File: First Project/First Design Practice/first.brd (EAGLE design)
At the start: 118.1 x 55.5 mm, 6 parts, among them U1 ARDUINOR3-BPLACE

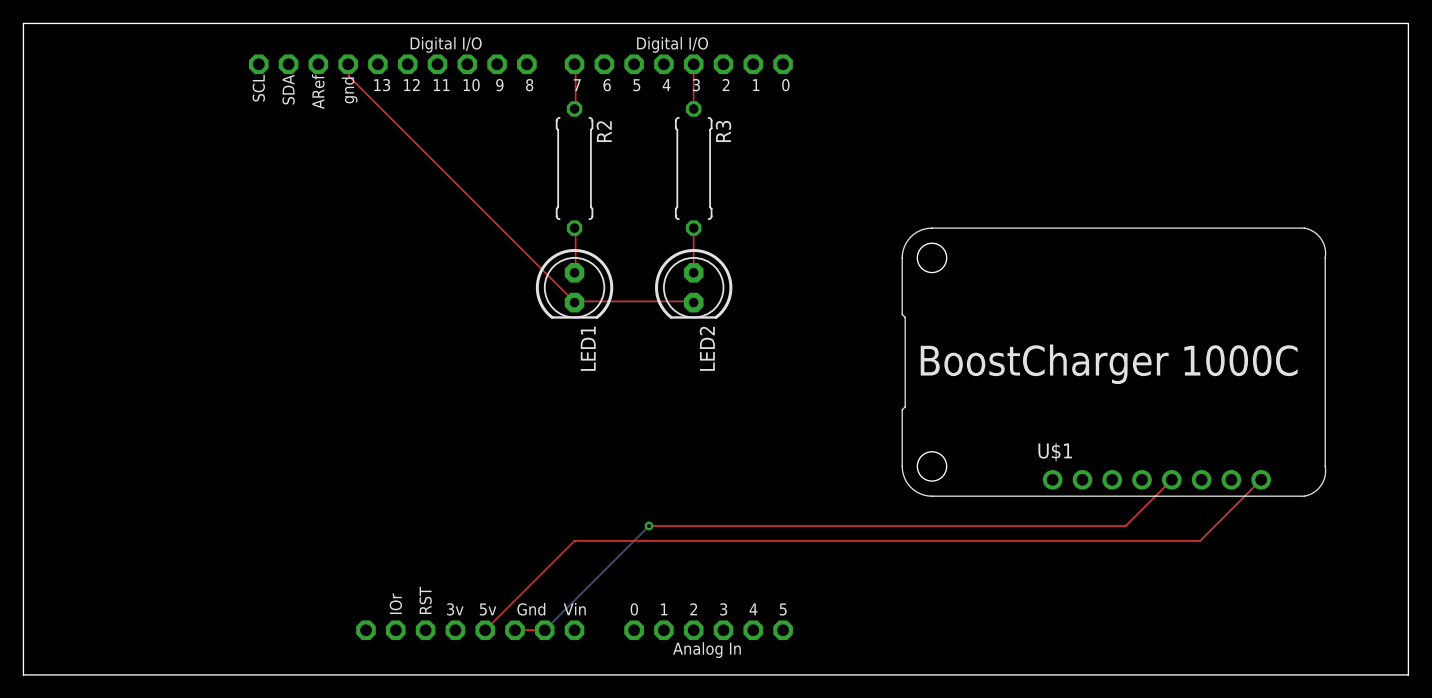
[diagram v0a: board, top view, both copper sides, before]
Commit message: Added Experimental Boards/ Gravity Board/ Home Automation Boards
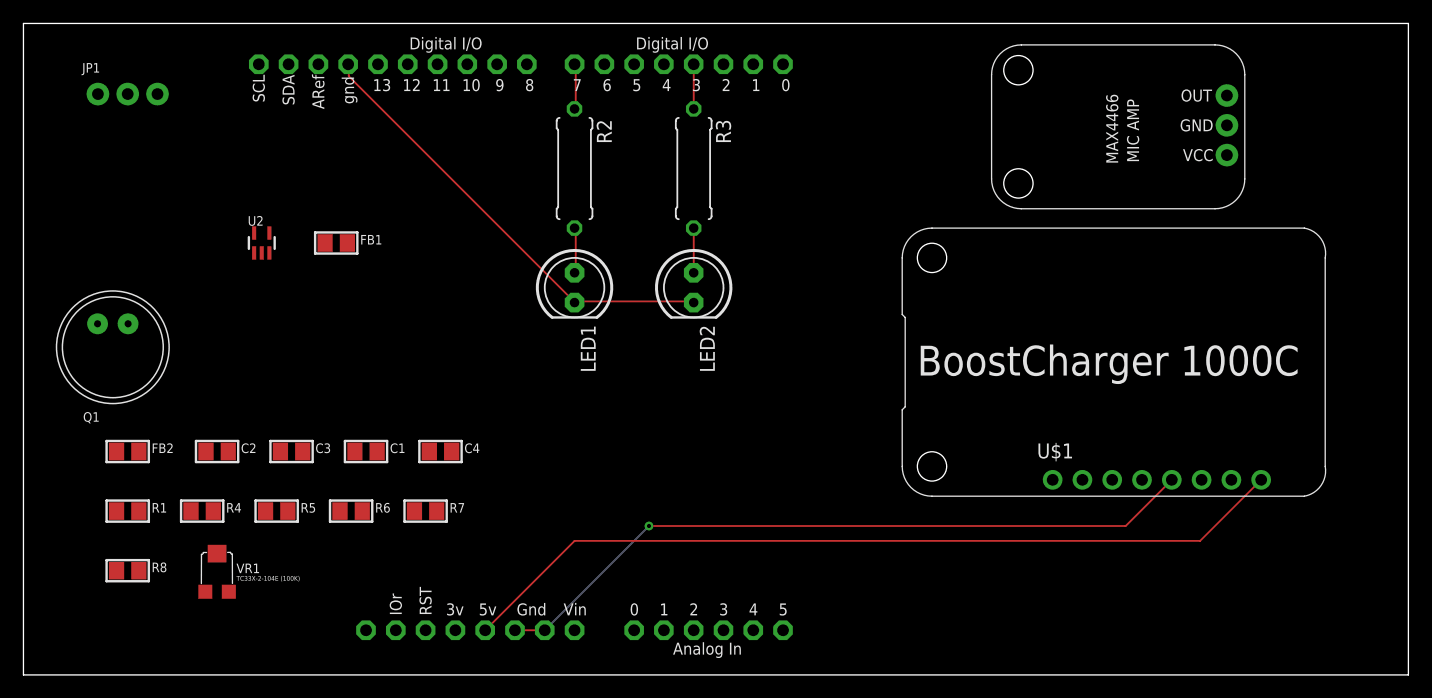
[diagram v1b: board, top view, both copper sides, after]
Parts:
- added C1: 0.1µF, microbuilder:0805
- added C2: 0.01uF, microbuilder:0805
- added C3: 100pF, microbuilder:0805
- added C4: 10uF, microbuilder:0805
- added FB1, FB2: FERRITE, microbuilder:0805
- added JP1: (no value), microbuilder:1X03_ROUND_76
- added Q1: CMA-4544PF-W, microbuilder:ELECTRET_9.7
- added R1, R4, R5: 1K, microbuilder:0805
- added R6, R7: 1M, microbuilder:0805
- added R8: 22K, microbuilder:0805
- added U$11: MAX4466-MIC-AMP, untitled:MAX4466
- added U2: MAX4466EXK+T, microbuilder:SC70-5
- added VR1: TC33X-2-104E (100K), microbuilder:TRIMPOT_BOURNS_TC33X-2
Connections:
- new net AGND: C1.2, C4.2, FB1.2, Q1.-, R6.1, U2.2
- new net AVCC: FB2.1, R4.2, R7.2, U2.5
- new net N$10: C4.1, R5.1
- new net N$11: R8.2, VR1.3
- new net N$4: C2.1, Q1.+, R1.1
- new net N$6: C1.1, R1.2, R4.1
- new net N$7: C2.2, R6.2, R7.1, U2.1
- new net N$8: C3.1, JP1.3, U2.4, VR1.1, VR1.2
- new net N$9: C3.2, R5.2, R8.1, U2.3
- new net VCC: FB2.2, JP1.1
- net GND: now also FB1.1, JP1.2
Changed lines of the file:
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@@
 <element name="U1" library="adafruit" library_urn="urn:adsk.eagle:library:420" package="ARDUINOR3-BPLACE" value="ARDUINOR3-BPLACE" x="1.27" y="1.27"/>
 <element name="U$1" library="MyCustomParts" package="ADAFRUIT-POWERBOOST-1000C" value="ADAFRUIT-POWERBOOST-1000C" x="74.93" y="15.24"/>
+<element name="U2" library="microbuilder" package="SC70-5" value="MAX4466EXK+T" x="20.32" y="36.83"/>
+<element name="FB1" library="microbuilder" package="0805" value="FERRITE" x="26.67" y="36.83"/>
+<element name="FB2" library="microbuilder" package="0805" value="FERRITE" x="8.89" y="19.05"/>
+<element name="Q1" library="microbuilder" package="ELECTRET_9.7" value="CMA-4544PF-W" x="7.62" y="27.94"/>
+<element name="R1" library="microbuilder" package="0805" value="1K" x="8.89" y="13.97"/>
+<element name="R4" library="microbuilder" package="0805" value="1K" x="15.24" y="13.97"/>
+<element name="C1" library="microbuilder" package="0805" value="0.1µF" x="29.21" y="19.05"/>
+<element name="C2" library="microbuilder" package="0805" value="0.01uF" x="16.51" y="19.05"/>
+<element name="R5" library="microbuilder" package="0805" value="1K" x="21.59" y="13.97"/>
+<element name="R6" library="microbuilder" package="0805" value="1M" x="27.94" y="13.97"/>
+<element name="R7" library="microbuilder" package="0805" value="1M" x="34.29" y="13.97"/>
+<element name="C3" library="microbuilder" package="0805" value="100pF" x="22.86" y="19.05"/>
+<element name="VR1" library="microbuilder" package="TRIMPOT_BOURNS_TC33X-2" value="TC33X-2-104E (100K)" x="16.51" y="8.89"/>
+<element name="R8" library="microbuilder" package="0805" value="22K" x="8.89" y="8.89"/>
+<element name="C4" library="microbuilder" package="0805" value="10uF" x="35.56" y="19.05"/>
+<element name="JP1" library="microbuilder" package="1X03_ROUND_76" value="" x="8.89" y="49.53"/>
+<element name="U$11" library="untitled" package="MAX4466" value="MAX4466-MIC-AMP" x="104.14" y="39.37" rot="R90"/>
 </elements>
 <signals>
@@
 <via x="53.34" y="12.7" extent="1-16" drill="0.35"/>
 <wire x1="53.34" y1="12.7" x2="44.45" y2="3.81" width="0.1524" layer="16"/>
+<contactref element="FB1" pad="1"/>
+<contactref element="JP1" pad="2"/>
 <wire x1="53.34" y1="12.7" x2="57.15" y2="31.75" width="0" layer="19" extent="1-1"/>
+<wire x1="25.72" y1="36.83" x2="41.91" y2="3.81" width="0" layer="19" extent="1-1"/>
+<wire x1="8.89" y1="49.53" x2="25.72" y2="36.83" width="0" layer="19" extent="1-1"/>
 </signal>
 <signal name="+5V">
@@
 <wire x1="46.99" y1="11.43" x2="100.33" y2="11.43" width="0.1524" layer="1"/>
 </signal>
+<signal name="VCC">
+<contactref element="FB2" pad="2"/>
+<contactref element="JP1" pad="1"/>
+<wire x1="6.35" y1="49.53" x2="9.84" y2="19.05" width="0" layer="19" extent="1-1"/>
+</signal>
+<signal name="N$4">
+<contactref element="Q1" pad="+"/>
+<contactref element="R1" pad="1"/>
+<contactref element="C2" pad="1"/>
+<wire x1="15.56" y1="19.05" x2="7.94" y2="13.97" width="0" layer="19" extent="1-1"/>
+<wire x1="8.92" y1="29.94" x2="15.56" y2="19.05" width="0" layer="19" extent="1-1"/>
+</signal>
+<signal name="N$6">
+<contactref element="R4" pad="1"/>
+<contactref element="R1" pad="2"/>
+<contactref element="C1" pad="1"/>
+<wire x1="14.29" y1="13.97" x2="9.84" y2="13.97" width="0" layer="19" extent="1-1"/>
+<wire x1="28.26" y1="19.05" x2="14.29" y2="13.97" width="0" layer="19" extent="1-1"/>
+</signal>
+<signal name="N$7">
+<contactref element="U2" pad="1"/>
+<contactref element="C2" pad="2"/>
+<contactref element="R6" pad="2"/>
+<contactref element="R7" pad="1"/>
+<wire x1="28.89" y1="13.97" x2="17.46" y2="19.05" width="0" layer="19" extent="1-1"/>
+<wire x1="33.34" y1="13.97" x2="28.89" y2="13.97" width="0" layer="19" extent="1-1"/>
+<wire x1="19.67" y1="35.98" x2="17.46" y2="19.05" width="0" layer="19" extent="1-1"/>
+</signal>
+<signal name="AVCC">
+<contactref element="FB2" pad="1"/>
+<contactref element="U2" pad="5"/>
+<contactref element="R4" pad="2"/>
+<contactref element="R7" pad="2"/>
+<wire x1="16.19" y1="13.97" x2="7.94" y2="19.05" width="0" layer="19" extent="1-1"/>
+<wire x1="35.24" y1="13.97" x2="16.19" y2="13.97" width="0" layer="19" extent="1-1"/>
+<wire x1="19.67" y1="37.68" x2="35.24" y2="13.97" width="0" layer="19" extent="1-1"/>
+</signal>
+<signal name="AGND">
+<contactref element="FB1" pad="2"/>
+<contactref element="C1" pad="2"/>
+<contactref element="Q1" pad="-"/>
+<contactref element="U2" pad="2"/>
+<contactref element="R6" pad="1"/>
+<contactref element="C4" pad="2"/>
+<wire x1="30.16" y1="19.05" x2="26.99" y2="13.97" width="0" layer="19" extent="1-1"/>
+<wire x1="36.51" y1="19.05" x2="30.16" y2="19.05" width="0" layer="19" extent="1-1"/>
+<wire x1="6.32" y1="29.94" x2="30.16" y2="19.05" width="0" layer="19" extent="1-1"/>
+<wire x1="20.32" y1="35.98" x2="6.32" y2="29.94" width="0" layer="19" extent="1-1"/>
+<wire x1="27.62" y1="36.83" x2="20.32" y2="35.98" width="0" layer="19" extent="1-1"/>
+</signal>
+<signal name="N$8">
+<contactref element="U2" pad="4"/>
+<contactref element="VR1" pad="2"/>
+<contactref element="C3" pad="1"/>
+<contactref element="JP1" pad="3"/>
+<contactref element="VR1" pad="1"/>
+<wire x1="16.51" y1="10.34" x2="15.51" y2="7.09" width="0" layer="19" extent="1-1"/>
+<wire x1="21.91" y1="19.05" x2="16.51" y2="10.34" width="0" layer="19" extent="1-1"/>
+<wire x1="20.97" y1="37.68" x2="21.91" y2="19.05" width="0" layer="19" extent="1-1"/>
+<wire x1="11.43" y1="49.53" x2="20.97" y2="37.68" width="0" layer="19" extent="1-1"/>
+</signal>
+<signal name="N$9">
+<contactref element="U2" pad="3"/>
+<contactref element="R5" pad="2"/>
+<contactref element="R8" pad="1"/>
+<contactref element="C3" pad="2"/>
+<wire x1="22.54" y1="13.97" x2="7.94" y2="8.89" width="0" layer="19" extent="1-1"/>
+<wire x1="23.81" y1="19.05" x2="22.54" y2="13.97" width="0" layer="19" extent="1-1"/>
+<wire x1="20.97" y1="35.98" x2="23.81" y2="19.05" width="0" layer="19" extent="1-1"/>
+</signal>
+<signal name="N$10">
+<contactref element="R5" pad="1"/>
+<contactref element="C4" pad="1"/>
+<wire x1="34.61" y1="19.05" x2="20.64" y2="13.97" width="0" layer="19" extent="1-1"/>
+</signal>
+<signal name="N$11">
+<contactref element="R8" pad="2"/>
+<contactref element="VR1" pad="3"/>
+<wire x1="17.51" y1="7.09" x2="9.84" y2="8.89" width="0" layer="19" extent="1-1"/>
+</signal>
 </signals>
